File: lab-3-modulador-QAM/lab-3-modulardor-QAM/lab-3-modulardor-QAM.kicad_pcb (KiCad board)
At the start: 2 copper layers, 59 parts, among them J1 señales I-Q, J3 Fuente, Q2 2N3904, U1 LM741, U2 LM741, U3 LM741, U4 MC1496, U5 MC1496, U6 LM741

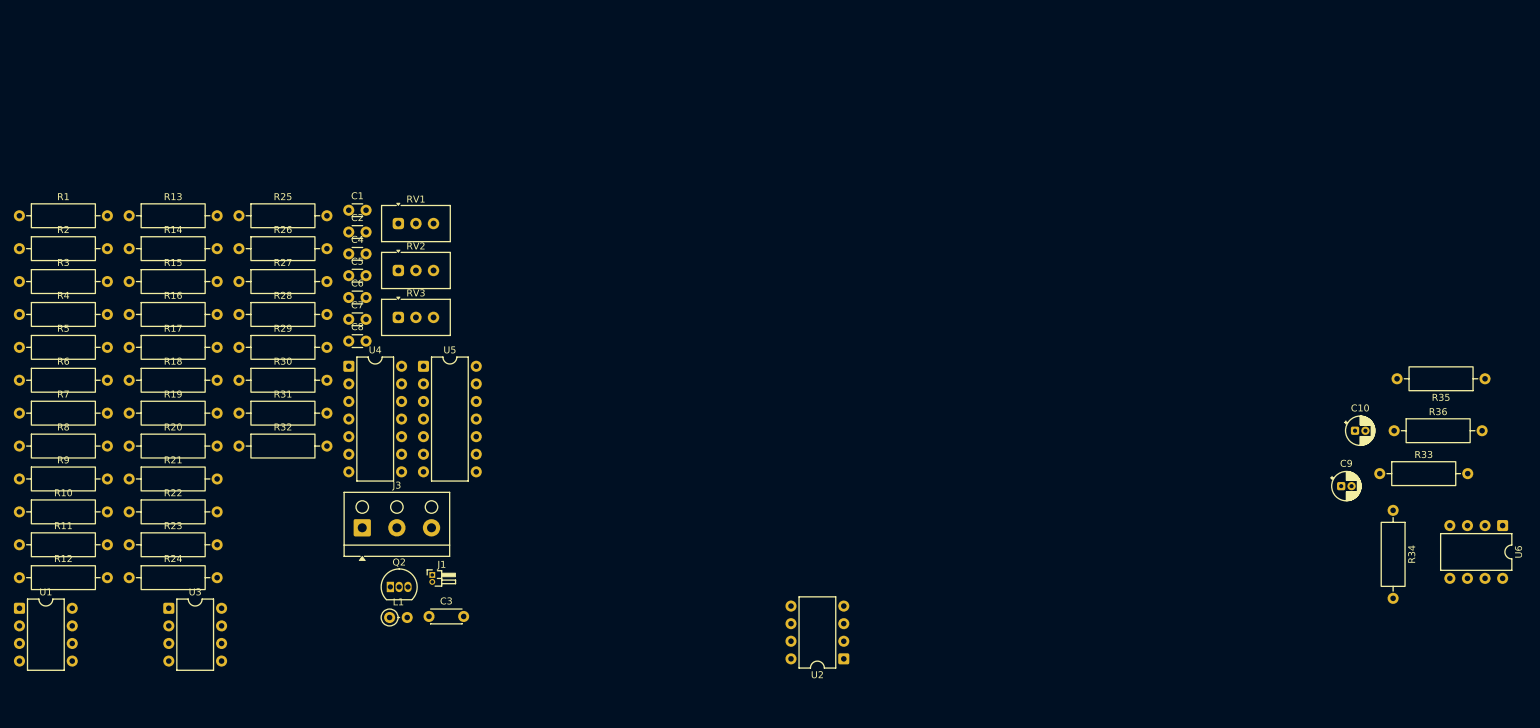
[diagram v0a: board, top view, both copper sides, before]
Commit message: Cambios en el esquematico, enrutado en pcb y correción de algunos errores
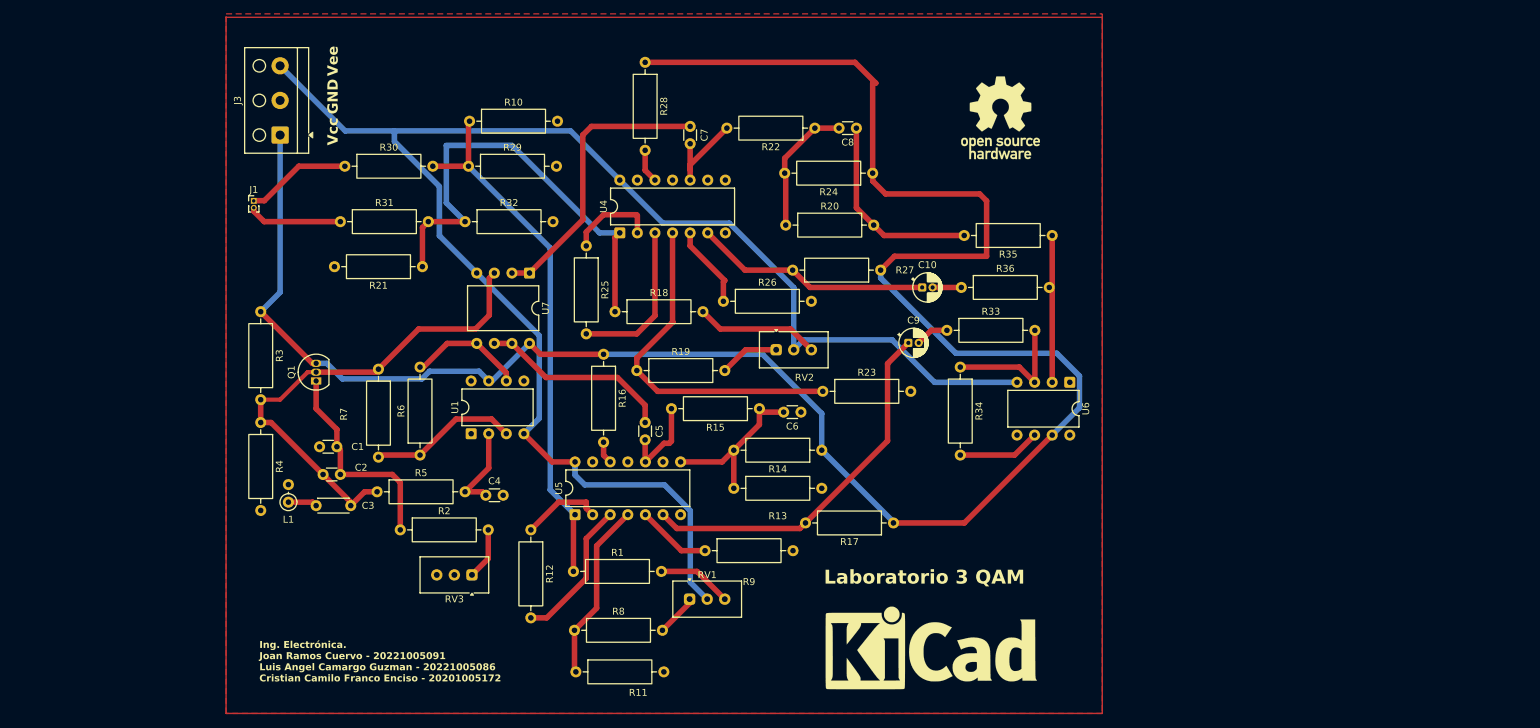
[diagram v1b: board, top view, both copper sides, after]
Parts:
- removed U2, U3: LM741, Package_DIP:DIP-8_W7.62mm
- added REF**: KiCad-Logo_12mm_SilkScreen, Symbol:KiCad-Logo_12mm_SilkScreen, F.Cu at (144.5, 142.5)
- added REF**: OSHW-Logo_11.4x12mm_SilkScreen, Symbol:OSHW-Logo_11.4x12mm_SilkScreen, F.Cu at (154.5, 66.0)
- added U7: LM358, Package_DIP:DIP-8_W10.16mm, F.Cu at (86.5, 88.4)
- J1: footprint Connector_PinHeader_1.00mm:PinHeader_1x02_P1.00mm_Horizontal -> Connector_PinHeader_1.00mm:PinHeader_1x02_P1.00mm_Vertical
- moved R24 122.2 mm to (136.1, 74.0), turned to 180 degrees
- moved R22 113.4 mm to (127.7, 67.5), turned to 180 degrees
- moved R17 113.2 mm to (139.1, 124.5), turned to 180 degrees
- moved R14 104.1 mm to (128.7, 114.0), turned to 180 degrees
- moved R23 102.6 mm to (128.8, 105.5)
- moved R20 100.0 mm to (123.5, 81.5)
- moved R9 99.5 mm to (111.8, 128.5)
- moved R13 95.7 mm to (116.0, 119.5)
- moved R1 95.1 mm to (92.8, 131.5)
- moved R15 92.8 mm to (119.7, 108.0), turned to 180 degrees
- moved R27 92.7 mm to (137.2, 88.0), turned to 180 degrees
- moved R10 86.1 mm to (77.8, 66.5)
- moved R8 84.4 mm to (93.0, 140.0)
- moved R11 82.4 mm to (93.2, 146.0)
- moved C8 79.5 mm to (133.7, 67.5), turned to 180 degrees
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- renumbered Q2 to Q1
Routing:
- net +12V: track 0.00 -> 304.1 mm
- net -12V: track 0.00 -> 228.6 mm
- net RI(t): track 0.00 -> 76.7 mm
- net sen(wt): track 0.00 -> 70.6 mm
- net RQ(t): track 0.00 -> 66.2 mm
- net RAI(t): track 0.00 -> 53.9 mm
- net Net-(R19-Pad1): track 0.00 -> 50.1 mm
- net Bsen(wt): track 0.00 -> 41.7 mm
- net RAQ(t): track 0.00 -> 34.2 mm
- net Net-(Q1-E): track 0.00 -> 30.9 mm
- net GND: track 0.00 -> 29.0 mm
- net Bcos(wt): track 0.00 -> 28.0 mm
- net Net-(R11-Pad1): track 0.00 -> 26.0 mm
- net Net-(C6-Pad2): track 0.00 -> 25.1 mm
- net Net-(R25-Pad2): track 0.00 -> 23.0 mm
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- added copper zone on F.Cu, net GND
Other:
- board text added: "GND"
- board text added: "Ing. Electrónica. Joan Ramos Cuervo - 20221005091 Luis Angel Camargo Guzman - 20221005086 Cristian Camilo Franco Enciso - 20201005172"
- board text added: "Laboratorio 3 QAM"
- board text added: "Vcc"
- board text added: "Vee"

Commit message: Separadando por partes. Oscilador y Modulador
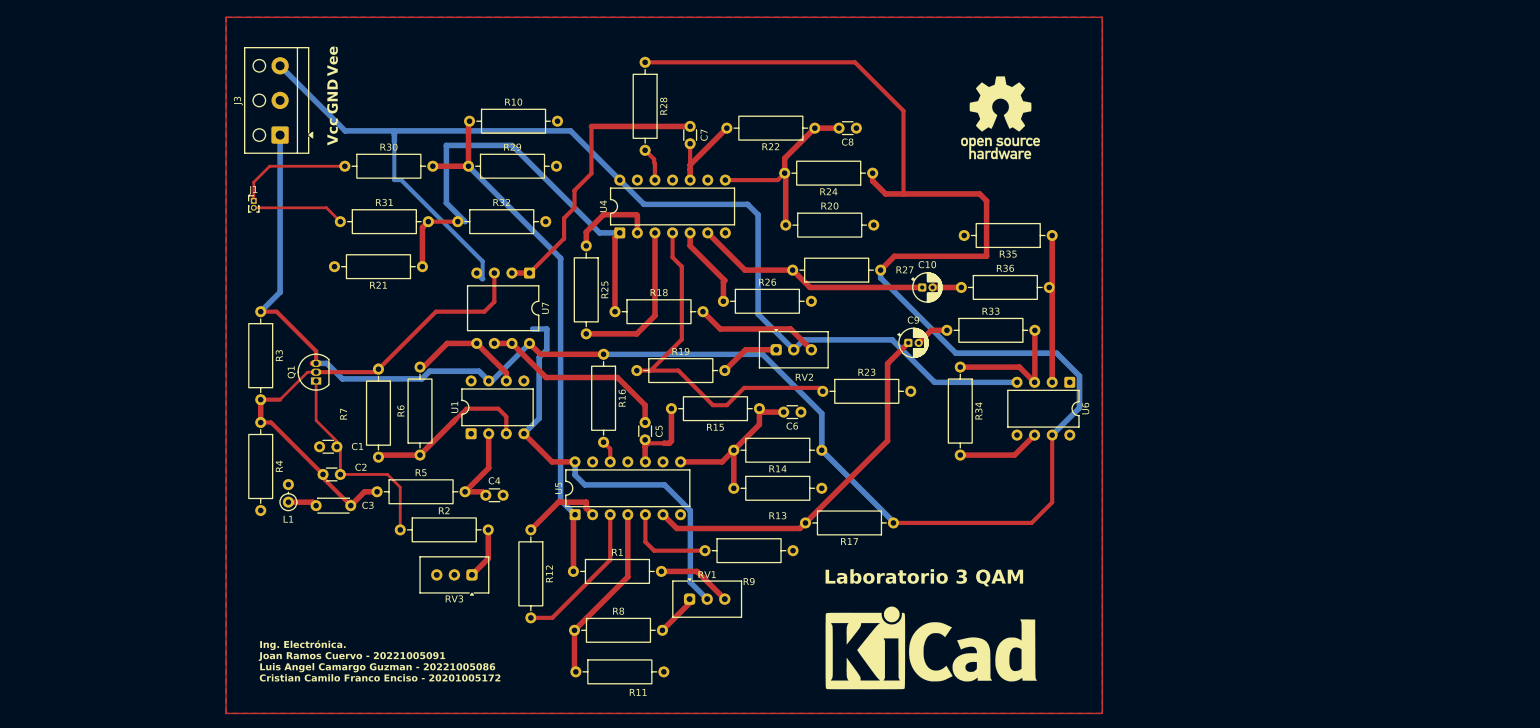
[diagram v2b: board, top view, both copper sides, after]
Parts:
- moved R32 1.05 mm to (76.2, 81.0)
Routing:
- net GND: track 29.0 -> 0.28 mm
- net +12V: track 304.1 -> 315.6 mm
- net Net-(C8-Pad2): track 19.4 -> 28.3 mm
- net Net-(U1-+): track 22.0 -> 25.4 mm
- net Net-(R19-Pad1): track 50.1 -> 52.5 mm
- net Net-(R9-Pad1): track 10.8 -> 13.1 mm
- net -12V: track 228.6 -> 226.3 mm
- net I(t): track 15.2 -> 16.8 mm
- net RQ(t): track 66.2 -> 65.2 mm
- net Net-(C5-Pad2): track 12.9 -> 12.1 mm
